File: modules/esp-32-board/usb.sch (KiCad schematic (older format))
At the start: 12 parts, among them J7 USB_B_Micro, Q1 BCR129S, U4 USBLC6-2SC6, U5 FT232RL

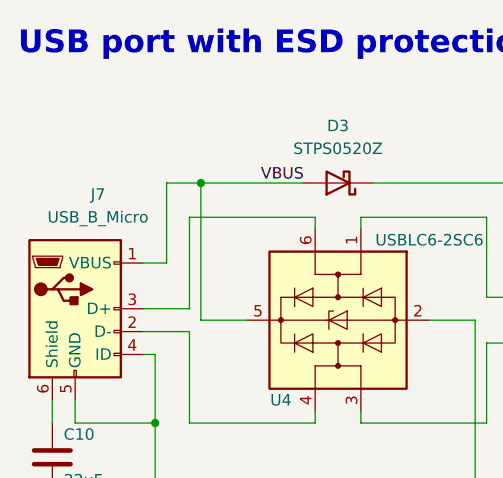
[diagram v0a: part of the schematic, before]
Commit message: Replace MainConnector with ArduinoFootprint and separate headers
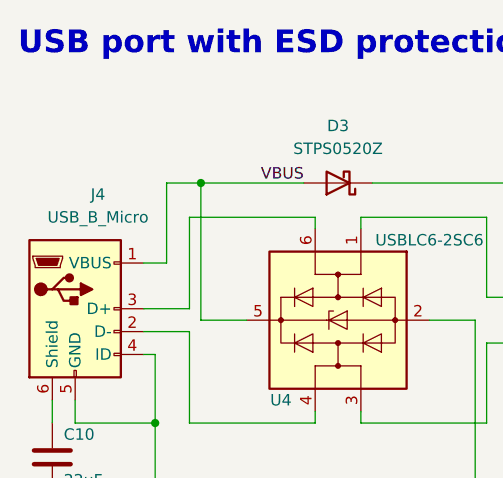
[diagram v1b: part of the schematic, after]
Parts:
- renumbered J7 to J4
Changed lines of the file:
@@
 P 1550 2750
 AR Path="/5FFC9948" Ref="J?"  Part="1"
-AR Path="/5FF73D59/5FFC9948" Ref="J7"  Part="1"
-F 0 "J7" H 1650 3250 50  0000 C CNN
+AR Path="/5FF73D59/5FFC9948" Ref="J4"  Part="1"
+F 0 "J4" H 1650 3250 50  0000 C CNN
 F 1 "USB_B_Micro" H 1650 3150 50  0000 C CNN
 F 2 "Connector_USB:USB_Micro-B_Amphenol_10118194_Horizontal" H 1700 2700 50  0001 C CNN

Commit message: Add custom symbols/footprints to project_components
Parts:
- Q1: symbol Transistor_BJT:BCR129S -> project_components:BCR129S
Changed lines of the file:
@@
 VBUS
 $Comp
-L Transistor_BJT:BCR129S Q1
+L project_components:BCR129S Q1
 U 1 1 5FB53DE1
 P 9900 2100
 F 0 "Q1" H 10050 2150 50  0000 L CNN
-F 1 "BCR129S" H 10050 2100 50  0000 L CNN
+F 1 "BCR129S" H 10050 2050 50  0000 L CNN
 F 2 "Package_TO_SOT_SMD:SOT-363_SC-70-6" H 9905 1660 50  0001 C CNN
 F 3 "https://www.infineon.com/dgdl/Infineon-BCR129SERIES-DS-v01_01-en.pdf?fileId=db3a30431428a37301143f7ab7820287" H 9900 2100 50  0001 C CNN
@@
 $EndComp
 $Comp
-L Transistor_BJT:BCR129S Q1
+L project_components:BCR129S Q1
 U 2 1 5FB59A80
 P 9900 2650
-F 0 "Q1" H 10050 2700 50  0000 L CNN
-F 1 "BCR129S" H 10050 2650 50  0000 L CNN
+F 0 "Q1" H 10050 2600 50  0000 L CNN
+F 1 "BCR129S" H 10050 2700 50  0000 L CNN
 F 2 "Package_TO_SOT_SMD:SOT-363_SC-70-6" H 9905 2210 50  0001 C CNN
 F 3 "https://www.infineon.com/dgdl/Infineon-BCR129SERIES-DS-v01_01-en.pdf?fileId=db3a30431428a37301143f7ab7820287" H 9900 2650 50  0001 C CNN

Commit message: Documentational changes
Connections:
- net USB_SHIELD: now reaches C10.1, J4.6 (Shield)
- net USB_RESET: now reaches R2.1, U5.19 (~RESET~)
- net USB_DN': now reaches J4.2 (D-), U4.4 (I/O2)
- net USB_DP': now reaches J4.3 (D+), U4.6 (I/O1)
- net ~TXDLED': now reaches D4.1 (K), R3.1
- net ~RXDLED': now reaches D5.1 (K), R4.1
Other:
- note added: "DTR RTS -> EN IO0\n 1 1 1 1\n 0 0 1 1\n 1 0 0 1\n 0 1 1 0"
- note added: "LEDs"
- note added: "Source: https://dl.espressif.com/dl/schematics/esp32_devkitc_v4-sch-20180607a.pdf"
- moved on the sheet: C10, C11, D3, D4, D5, J4, Q1A, Q1B, R2, R3, R4, U4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
